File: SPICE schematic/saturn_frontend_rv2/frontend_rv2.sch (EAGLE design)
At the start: 32 parts

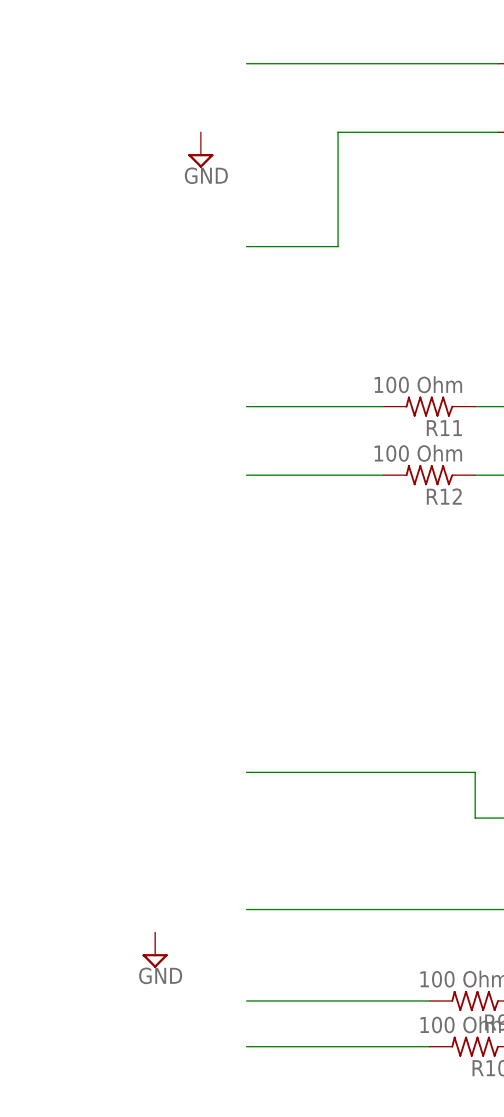
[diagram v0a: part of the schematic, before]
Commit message: Eagle Board RV3 added with updated component names
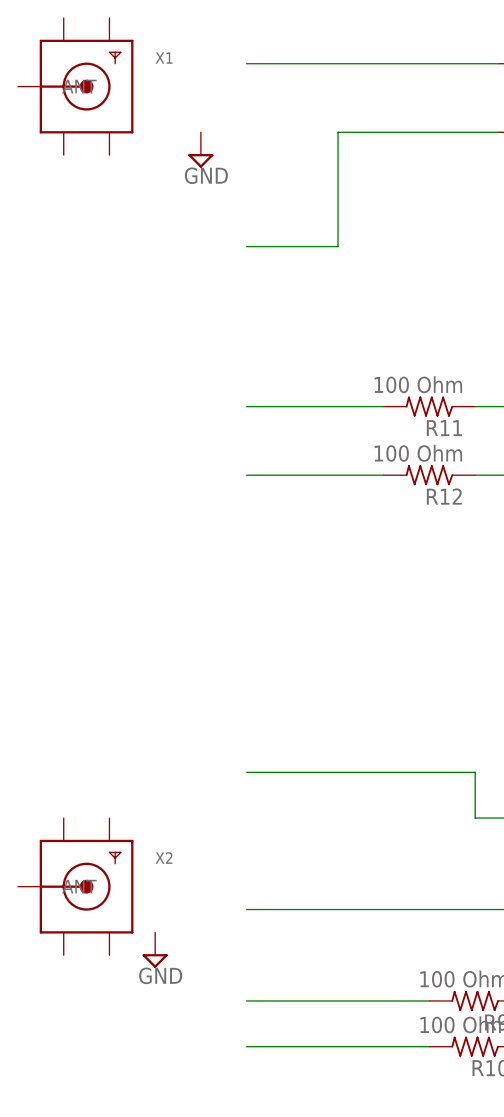
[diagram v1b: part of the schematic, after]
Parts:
- added X1, X2: (no value), adafruit:SMACONNECTOR_EDGE
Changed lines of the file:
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@@
 <layer number="48" name="Document" color="7" fill="1" visible="no" active="no"/>
 <layer number="49" name="Reference" color="7" fill="1" visible="no" active="no"/>
+<layer number="50" name="dxf" color="7" fill="1" visible="no" active="no"/>
 <layer number="51" name="tDocu" color="6" fill="1" visible="no" active="no"/>
 <layer number="52" name="bDocu" color="7" fill="1" visible="no" active="no"/>
+<layer number="53" name="tGND_GNDA" color="7" fill="9" visible="no" active="no"/>
+<layer number="54" name="bGND_GNDA" color="1" fill="9" visible="no" active="no"/>
+<layer number="56" name="wert" color="7" fill="1" visible="no" active="no"/>
+<layer number="57" name="tCAD" color="7" fill="1" visible="no" active="no"/>
+<layer number="59" name="tCarbon" color="7" fill="1" visible="no" active="no"/>
+<layer number="60" name="bCarbon" color="7" fill="1" visible="no" active="no"/>
 <layer number="90" name="Modules" color="5" fill="1" visible="yes" active="yes"/>
 <layer number="91" name="Nets" color="2" fill="1" visible="yes" active="yes"/>
@@
 <layer number="98" name="Guide" color="6" fill="1" visible="yes" active="yes"/>
 <layer number="99" name="SpiceOrder" color="5" fill="1" visible="yes" active="yes"/>
+<layer number="100" name="Muster" color="7" fill="1" visible="no" active="no"/>
+<layer number="101" name="Patch_Top" color="12" fill="4" visible="no" active="yes"/>
+<layer number="102" name="Vscore" color="7" fill="1" visible="no" active="yes"/>
+<layer number="103" name="fp3" color="7" fill="1" visible="no" active="yes"/>
+<layer number="104" name="Name" color="7" fill="1" visible="no" active="yes"/>
+<layer number="105" name="Beschreib" color="9" fill="1" visible="no" active="yes"/>
+<layer number="106" name="BGA-Top" color="4" fill="1" visible="no" active="yes"/>
+<layer number="107" name="BD-Top" color="5" fill="1" visible="no" active="yes"/>
+<layer number="108" name="fp8" color="7" fill="1" visible="no" active="yes"/>
+<layer number="109" name="fp9" color="7" fill="1" visible="no" active="yes"/>
+<layer number="110" name="fp0" color="7" fill="1" visible="no" active="yes"/>
+<layer number="111" name="LPC17xx" color="7" fill="1" visible="no" active="yes"/>
+<layer number="112" name="tSilk" color="7" fill="1" visible="no" active="yes"/>
+<layer number="113" name="ReferenceLS" color="7" fill="1" visible="no" active="no"/>
+<layer number="116" name="Patch_BOT" color="9" fill="4" visible="no" active="yes"/>
+<layer number="118" name="Rect_Pads" color="7" fill="1" visible="no" active="no"/>
+<layer number="121" name="_tsilk" color="7" fill="1" visible="no" active="yes"/>
+<layer number="122" name="_bsilk" color="7" fill="1" visible="no" active="yes"/>
+<layer number="123" name="tTestmark" color="7" fill="1" visible="no" active="yes"/>
+<layer number="124" name="bTestmark" color="7" fill="1" visible="no" active="yes"/>
+<layer number="125" name="_tNames" color="7" fill="1" visible="no" active="yes"/>
+<layer number="126" name="_bNames" color="7" fill="1" visible="no" active="yes"/>
+<layer number="127" name="_tValues" color="7" fill="1" visible="no" active="yes"/>
+<layer number="128" name="_bValues" color="7" fill="1" visible="no" active="yes"/>
+<layer number="129" name="Mask" color="7" fill="1" visible="yes" active="yes"/>
+<layer number="131" name="tAdjust" color="7" fill="1" visible="no" active="yes"/>
+<layer number="132" name="bAdjust" color="7" fill="1" visible="no" active="yes"/>
+<layer number="144" name="Drill_legend" color="7" fill="1" visible="no" active="yes"/>
+<layer number="150" name="Notes" color="7" fill="1" visible="no" active="yes"/>
+<layer number="151" name="HeatSink" color="7" fill="1" visible="no" active="yes"/>
+<layer number="152" name="_bDocu" color="7" fill="1" visible="no" active="yes"/>
+<layer number="153" name="FabDoc1" color="6" fill="1" visible="no" active="no"/>
+<layer number="154" name="FabDoc2" color="2" fill="1" visible="no" active="no"/>
+<layer number="155" name="FabDoc3" color="7" fill="15" visible="no" active="no"/>
+<layer number="199" name="Contour" color="7" fill="1" visible="no" active="yes"/>
+<layer number="200" name="200bmp" color="1" fill="10" visible="no" active="yes"/>
+<layer number="201" name="201bmp" color="2" fill="1" visible="no" active="no"/>
+<layer number="202" name="202bmp" color="3" fill="1" visible="no" active="no"/>
+<layer number="203" name="203bmp" color="4" fill="10" visible="no" active="yes"/>
+<layer number="204" name="204bmp" color="5" fill="10" visible="no" active="yes"/>
+<layer number="205" name="205bmp" color="6" fill="10" visible="no" active="yes"/>
+<layer number="206" name="206bmp" color="7" fill="10" visible="no" active="yes"/>
+<layer number="207" name="207bmp" color="8" fill="10" visible="no" active="yes"/>
+<layer number="208" name="208bmp" color="9" fill="10" visible="no" active="yes"/>
+<layer number="209" name="209bmp" color="7" fill="1" visible="no" active="yes"/>
+<layer number="210" name="210bmp" color="7" fill="1" visible="no" active="yes"/>
+<layer number="211" name="211bmp" color="7" fill="1" visible="no" active="yes"/>
+<layer number="212" name="212bmp" color="7" fill="1" visible="no" active="yes"/>
+<layer number="213" name="213bmp" color="7" fill="1" visible="no" active="yes"/>
+<layer number="214" name="214bmp" color="7" fill="1" visible="no" active="yes"/>
+<layer number="215" name="215bmp" color="7" fill="1" visible="no" active="yes"/>
+<layer number="216" name="216bmp" color="7" fill="1" visible="no" active="yes"/>
+<layer number="217" name="217bmp" color="18" fill="1" visible="no" active="no"/>
+<layer number="218" name="218bmp" color="19" fill="1" visible="no" active="no"/>
+<layer number="219" name="219bmp" color="20" fill="1" visible="no" active="no"/>
+<layer number="220" name="220bmp" color="21" fill="1" visible="no" active="no"/>
+<layer number="221" name="221bmp" color="22" fill="1" visible="no" active="no"/>
+<layer number="222" name="222bmp" color="23" fill="1" visible="no" active="no"/>
+<layer number="223" name="223bmp" color="24" fill="1" visible="no" active="no"/>
+<layer number="224" name="224bmp" color="25" fill="1" visible="no" active="no"/>
+<layer number="225" name="225bmp" color="7" fill="1" visible="yes" active="yes"/>
+<layer number="226" name="226bmp" color="7" fill="1" visible="yes" active="yes"/>
+<layer number="227" name="227bmp" color="7" fill="1" visible="yes" active="yes"/>
+<layer number="228" name="228bmp" color="7" fill="1" visible="yes" active="yes"/>
+<layer number="229" name="229bmp" color="7" fill="1" visible="yes" active="yes"/>
+<layer number="230" name="230bmp" color="7" fill="1" visible="yes" active="yes"/>
+<layer number="231" name="Eagle3D_PG1" color="7" fill="1" visible="no" active="no"/>
+<layer number="232" name="Eagle3D_PG2" color="7" fill="1" visible="no" active="no"/>
+<layer number="233" name="Eagle3D_PG3" color="7" fill="1" visible="no" active="no"/>
+<layer number="248" name="Housing" color="7" fill="1" visible="no" active="yes"/>
+<layer number="249" name="Edge" color="7" fill="1" visible="no" active="yes"/>
+<layer number="250" name="Descript" color="7" fill="1" visible="no" active="no"/>
+<layer number="251" name="SMDround" color="7" fill="1" visible="no" active="no"/>
+<layer number="254" name="cooling" color="7" fill="1" visible="no" active="yes"/>
+<layer number="255" name="routoute" color="7" fill="1" visible="yes" active="yes"/>
 </layers>
 <schematic xreflabel="%F%N/%S.%C%R" xrefpart="/%S.%C%R">
@@
 <part name="SUPPLY9" library="supply2" deviceset="GND" device=""/>
 <part name="SUPPLY10" library="supply2" deviceset="GND" device=""/>
+<part name="X1" library="adafruit" deviceset="SMACONNECTOR" device="_EDGE"/>
+<part name="X2" library="adafruit" deviceset="SMACONNECTOR" device="_EDGE"/>
 </parts>
 <sheets>
@@
 <instance part="SUPPLY9" gate="GND" x="53.34" y="58.42"/>
 <instance part="SUPPLY10" gate="GND" x="60.96" y="58.42"/>
+<instance part="X1" gate="G$1" x="-15.24" y="111.76"/>
+<instance part="X2" gate="G$1" x="-15.24" y="22.86"/>
 </instances>
 <busses>
